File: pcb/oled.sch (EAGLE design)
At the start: 20 parts, among them U1 UG-2828GDEDF11, U2 FAN5331SX

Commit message: changed part number for pin header on oled board
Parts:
- JP1, JP2: BOTTOM (none) -> 0; MPN 10129378-908001BLF -> C124381; POPULATE 0 -> 1; THRU-HOLE (none) -> 1
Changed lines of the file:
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@@
 <?xml version="1.0" encoding="utf-8"?>
 <!DOCTYPE eagle SYSTEM "eagle.dtd">
-<eagle version="9.6.2">
+<eagle version="9.5.0">
 <drawing>
 <settings>
@@
 </part>
 <part name="JP2" library="adafruit" library_urn="urn:adsk.eagle:library:420" deviceset="PINHD-1X8" device="CLEANBIG" package3d_urn="urn:adsk.eagle:package:6240708/1" override_package3d_urn="urn:adsk.eagle:package:21520305/2" override_package_urn="urn:adsk.eagle:footprint:6240062/1">
-<attribute name="MPN" value="10129378-908001BLF"/>
-<attribute name="POPULATE" value="0"/>
+<attribute name="BOTTOM" value="0"/>
+<attribute name="MPN" value="C124381"/>
+<attribute name="POPULATE" value="1"/>
+<attribute name="THRU-HOLE" value="1"/>
 </part>
 <part name="JP1" library="adafruit" library_urn="urn:adsk.eagle:library:420" deviceset="PINHD-1X8" device="CLEANBIG" package3d_urn="urn:adsk.eagle:package:6240708/1" override_package3d_urn="urn:adsk.eagle:package:21520308/2" override_package_urn="urn:adsk.eagle:footprint:6240062/1">
-<attribute name="MPN" value="10129378-908001BLF"/>
-<attribute name="POPULATE" value="0"/>
+<attribute name="BOTTOM" value="0"/>
+<attribute name="MPN" value="C124381"/>
+<attribute name="POPULATE" value="1"/>
+<attribute name="THRU-HOLE" value="1"/>
 </part>
 <part name="SUPPLY1" library="SparkFun-PowerSymbols" library_urn="urn:adsk.eagle:library:530" deviceset="VIN" device=""/>
@@
 <attribute name="POPULATE" x="226.06" y="91.44" size="1.778" layer="96" rot="R180" display="off"/>
 <attribute name="MPN" x="226.06" y="91.44" size="1.778" layer="96" rot="R180" display="off"/>
+<attribute name="THRU-HOLE" x="226.06" y="91.44" size="1.778" layer="96" rot="R180" display="off"/>
+<attribute name="BOTTOM" x="226.06" y="91.44" size="1.778" layer="96" rot="R180" display="off"/>
 </instance>
 <instance part="JP1" gate="G$1" x="215.9" y="93.98" smashed="yes">
@@
 <attribute name="POPULATE" x="215.9" y="93.98" size="1.778" layer="96" display="off"/>
 <attribute name="MPN" x="215.9" y="93.98" size="1.778" layer="96" display="off"/>
+<attribute name="THRU-HOLE" x="215.9" y="93.98" size="1.778" layer="96" display="off"/>
+<attribute name="BOTTOM" x="215.9" y="93.98" size="1.778" layer="96" display="off"/>
 </instance>
 <instance part="SUPPLY1" gate="G$1" x="193.04" y="177.8" smashed="yes">

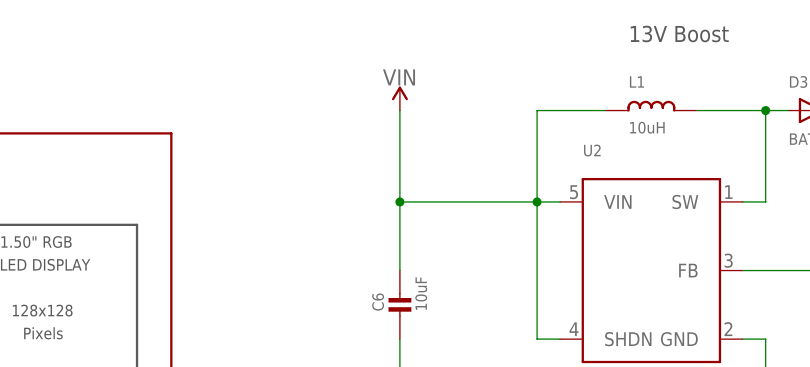
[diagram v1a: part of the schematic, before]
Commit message: Revert OLED board to use 3.3V for input to the 13V FAN5331 boost
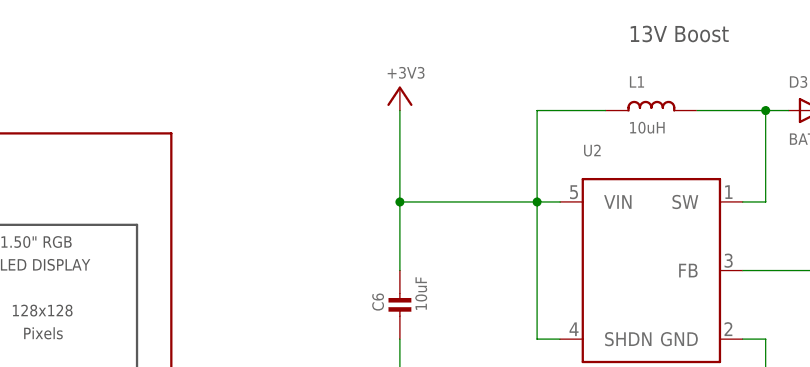
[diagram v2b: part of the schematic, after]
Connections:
- net +3V3: now also C6.P$1, L1.1, U2.SHDN, U2.VIN
- net VIN: no longer C6.P$1, L1.1, U2.SHDN, U2.VIN
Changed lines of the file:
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@@
 <?xml version="1.0" encoding="utf-8"?>
 <!DOCTYPE eagle SYSTEM "eagle.dtd">
-<eagle version="9.5.0">
+<eagle version="9.6.2">
 <drawing>
 <settings>
@@
 <attribute name="THRU-HOLE" value="1"/>
 </part>
-<part name="SUPPLY1" library="SparkFun-PowerSymbols" library_urn="urn:adsk.eagle:library:530" deviceset="VIN" device=""/>
+<part name="+3V1" library="supply1" library_urn="urn:adsk.eagle:library:371" deviceset="+3V3" device=""/>
 </parts>
 <sheets>
@@
 <attribute name="BOTTOM" x="215.9" y="93.98" size="1.778" layer="96" display="off"/>
 </instance>
-<instance part="SUPPLY1" gate="G$1" x="193.04" y="177.8" smashed="yes">
-<attribute name="VALUE" x="193.04" y="180.594" size="1.778" layer="96" align="bottom-center"/>
+<instance part="+3V1" gate="G$1" x="193.04" y="180.34" smashed="yes">
+<attribute name="VALUE" x="191.516" y="181.356" size="1.27" layer="96"/>
 </instance>
 </instances>
@@
 <pinref part="U1" gate="G$1" pin="VCI"/>
 </segment>
-</net>
-<net name="D1/GPIO5" class="0">
-<segment>
-<pinref part="JP1" gate="G$1" pin="3"/>
-<wire x1="213.36" y1="96.52" x2="203.2" y2="96.52" width="0.1524" layer="91"/>
-<label x="203.2" y="96.52" size="1.778" layer="95" rot="R180"/>
-</segment>
-</net>
-<net name="D2/GPIO4" class="0">
-<segment>
-<pinref part="JP1" gate="G$1" pin="4"/>
-<wire x1="213.36" y1="93.98" x2="203.2" y2="93.98" width="0.1524" layer="91"/>
-<label x="203.2" y="93.98" size="1.778" layer="95" rot="R180"/>
-</segment>
-</net>
-<net name="D3/GPIO0" class="0">
-<segment>
-<pinref part="JP1" gate="G$1" pin="5"/>
-<wire x1="213.36" y1="91.44" x2="203.2" y2="91.44" width="0.1524" layer="91"/>
-<label x="203.2" y="91.44" size="1.778" layer="95" rot="R180"/>
-</segment>
-</net>
-<net name="D4/GPIO2" class="0">
-<segment>
-<pinref part="JP1" gate="G$1" pin="6"/>
-<wire x1="213.36" y1="88.9" x2="203.2" y2="88.9" width="0.1524" layer="91"/>
-<label x="203.2" y="88.9" size="1.778" layer="95" rot="R180"/>
-</segment>
-<segment>
-<wire x1="129.54" y1="124.46" x2="111.76" y2="124.46" width="0.1524" layer="91"/>
-<label x="111.76" y="124.46" size="1.778" layer="95"/>
-<pinref part="U1" gate="G$1" pin="D/C#"/>
-</segment>
-</net>
-<net name="D8/GPIO15" class="0">
-<segment>
-<pinref part="JP2" gate="G$1" pin="2"/>
-<wire x1="228.6" y1="86.36" x2="238.76" y2="86.36" width="0.1524" layer="91"/>
-<label x="238.76" y="86.36" size="1.778" layer="95"/>
-</segment>
-<segment>
-<wire x1="129.54" y1="121.92" x2="111.76" y2="121.92" width="0.1524" layer="91"/>
-<label x="111.76" y="121.92" size="1.778" layer="95"/>
-<pinref part="U1" gate="G$1" pin="RES#"/>
-</segment>
-</net>
-<net name="D5/GPIO14/SCK" class="0">
-<segment>
-<pinref part="JP2" gate="G$1" pin="5"/>
-<wire x1="228.6" y1="93.98" x2="238.76" y2="93.98" width="0.1524" layer="91"/>
-<label x="238.76" y="93.98" size="1.778" layer="95"/>
-</segment>
-<segment>
-<wire x1="129.54" y1="139.7" x2="111.76" y2="139.7" width="0.1524" layer="91"/>
-<label x="111.76" y="139.7" size="1.778" layer="95"/>
-<pinref part="U1" gate="G$1" pin="D0/SCK"/>
-</segment>
-</net>
-<net name="D0/GPIO16" class="0">
-<segment>
-<pinref part="JP2" gate="G$1" pin="6"/>
-<wire x1="228.6" y1="96.52" x2="238.76" y2="96.52" width="0.1524" layer="91"/>
-<label x="238.76" y="96.52" size="1.778" layer="95"/>
-</segment>
-<segment>
-<wire x1="129.54" y1="127" x2="111.76" y2="127" width="0.1524" layer="91"/>
-<label x="111.76" y="127" size="1.778" layer="95"/>
-<pinref part="U1" gate="G$1" pin="CS#"/>
-</segment>
-</net>
-<net name="A0" class="0">
-<segment>
-<pinref part="JP2" gate="G$1" pin="7"/>
-<wire x1="228.6" y1="99.06" x2="238.76" y2="99.06" width="0.1524" layer="91"/>
-<label x="238.76" y="99.06" size="1.778" layer="95"/>
-</segment>
-</net>
-<net name="D7/GPIO13/MOSI" class="0">
-<segment>
-<pinref part="JP2" gate="G$1" pin="3"/>
-<wire x1="228.6" y1="88.9" x2="238.76" y2="88.9" width="0.1524" layer="91"/>
-<label x="238.76" y="88.9" size="1.778" layer="95"/>
-</segment>
-<segment>
-<wire x1="129.54" y1="142.24" x2="111.76" y2="142.24" width="0.1524" layer="91"/>
-<label x="111.76" y="142.24" size="1.778" layer="95"/>
-<pinref part="U1" gate="G$1" pin="D1/SDIN"/>
-</segment>
-</net>
-<net name="VIN" class="1">
 <segment>
 <wire x1="193.04" y1="167.64" x2="193.04" y2="160.02" width="0.1524" layer="91"/>
@@
 <pinref part="U2" gate="G$1" pin="SHDN"/>
 <pinref part="L1" gate="G$1" pin="1"/>
-<pinref part="SUPPLY1" gate="G$1" pin="VIN"/>
-</segment>
+<pinref part="+3V1" gate="G$1" pin="+3V3"/>
+</segment>
+</net>
+<net name="D1/GPIO5" class="0">
+<segment>
+<pinref part="JP1" gate="G$1" pin="3"/>
+<wire x1="213.36" y1="96.52" x2="203.2" y2="96.52" width="0.1524" layer="91"/>
+<label x="203.2" y="96.52" size="1.778" layer="95" rot="R180"/>
+</segment>
+</net>
+<net name="D2/GPIO4" class="0">
+<segment>
+<pinref part="JP1" gate="G$1" pin="4"/>
+<wire x1="213.36" y1="93.98" x2="203.2" y2="93.98" width="0.1524" layer="91"/>
+<label x="203.2" y="93.98" size="1.778" layer="95" rot="R180"/>
+</segment>
+</net>
+<net name="D3/GPIO0" class="0">
+<segment>
+<pinref part="JP1" gate="G$1" pin="5"/>
+<wire x1="213.36" y1="91.44" x2="203.2" y2="91.44" width="0.1524" layer="91"/>
+<label x="203.2" y="91.44" size="1.778" layer="95" rot="R180"/>
+</segment>
+</net>
+<net name="D4/GPIO2" class="0">
+<segment>
+<pinref part="JP1" gate="G$1" pin="6"/>
+<wire x1="213.36" y1="88.9" x2="203.2" y2="88.9" width="0.1524" layer="91"/>
+<label x="203.2" y="88.9" size="1.778" layer="95" rot="R180"/>
+</segment>
+<segment>
+<wire x1="129.54" y1="124.46" x2="111.76" y2="124.46" width="0.1524" layer="91"/>
+<label x="111.76" y="124.46" size="1.778" layer="95"/>
+<pinref part="U1" gate="G$1" pin="D/C#"/>
+</segment>
+</net>
+<net name="D8/GPIO15" class="0">
+<segment>
+<pinref part="JP2" gate="G$1" pin="2"/>
+<wire x1="228.6" y1="86.36" x2="238.76" y2="86.36" width="0.1524" layer="91"/>
+<label x="238.76" y="86.36" size="1.778" layer="95"/>
+</segment>
+<segment>
+<wire x1="129.54" y1="121.92" x2="111.76" y2="121.92" width="0.1524" layer="91"/>
+<label x="111.76" y="121.92" size="1.778" layer="95"/>
+<pinref part="U1" gate="G$1" pin="RES#"/>
+</segment>
+</net>
+<net name="D5/GPIO14/SCK" class="0">
+<segment>
+<pinref part="JP2" gate="G$1" pin="5"/>
+<wire x1="228.6" y1="93.98" x2="238.76" y2="93.98" width="0.1524" layer="91"/>
+<label x="238.76" y="93.98" size="1.778" layer="95"/>
+</segment>
+<segment>
+<wire x1="129.54" y1="139.7" x2="111.76" y2="139.7" width="0.1524" layer="91"/>
+<label x="111.76" y="139.7" size="1.778" layer="95"/>
+<pinref part="U1" gate="G$1" pin="D0/SCK"/>
+</segment>
+</net>
+<net name="D0/GPIO16" class="0">
+<segment>
+<pinref part="JP2" gate="G$1" pin="6"/>
+<wire x1="228.6" y1="96.52" x2="238.76" y2="96.52" width="0.1524" layer="91"/>
+<label x="238.76" y="96.52" size="1.778" layer="95"/>
+</segment>
+<segment>
+<wire x1="129.54" y1="127" x2="111.76" y2="127" width="0.1524" layer="91"/>
+<label x="111.76" y="127" size="1.778" layer="95"/>
+<pinref part="U1" gate="G$1" pin="CS#"/>
+</segment>
+</net>
+<net name="A0" class="0">
+<segment>
+<pinref part="JP2" gate="G$1" pin="7"/>
+<wire x1="228.6" y1="99.06" x2="238.76" y2="99.06" width="0.1524" layer="91"/>
+<label x="238.76" y="99.06" size="1.778" layer="95"/>
+</segment>
+</net>
+<net name="D7/GPIO13/MOSI" class="0">
+<segment>
+<pinref part="JP2" gate="G$1" pin="3"/>
+<wire x1="228.6" y1="88.9" x2="238.76" y2="88.9" width="0.1524" layer="91"/>
+<label x="238.76" y="88.9" size="1.778" layer="95"/>
+</segment>
+<segment>
+<wire x1="129.54" y1="142.24" x2="111.76" y2="142.24" width="0.1524" layer="91"/>
+<label x="111.76" y="142.24" size="1.778" layer="95"/>
+<pinref part="U1" gate="G$1" pin="D1/SDIN"/>
+</segment>
+</net>
+<net name="VIN" class="1">
 <segment>
 <pinref part="JP1" gate="G$1" pin="8"/>

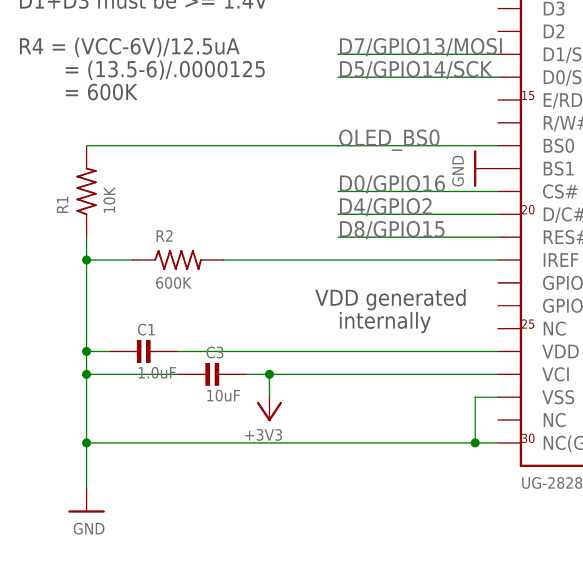
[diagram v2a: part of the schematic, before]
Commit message: changed 590k resistor to 620k
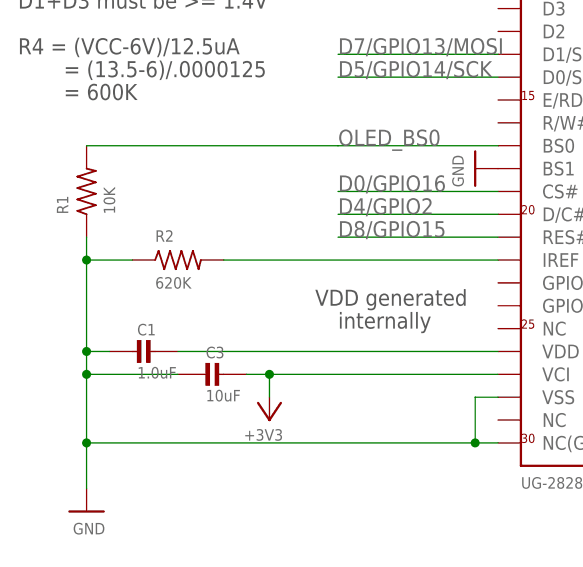
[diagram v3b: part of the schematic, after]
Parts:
- R2: value 600K -> 620K; MPN ERJ-6ENF5903V -> 0805W8F6203T5E
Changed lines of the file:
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@@
 <?xml version="1.0" encoding="utf-8"?>
 <!DOCTYPE eagle SYSTEM "eagle.dtd">
-<eagle version="9.6.2">
+<eagle version="9.5.0">
 <drawing>
 <settings>
@@
 <parts>
 <part name="GND2" library="supply1" library_urn="urn:adsk.eagle:library:371" deviceset="GND" device=""/>
-<part name="R2" library="adafruit" library_urn="urn:adsk.eagle:library:420" deviceset="R-US_" device="R0805" package3d_urn="urn:adsk.eagle:package:6240566/1" override_package3d_urn="urn:adsk.eagle:package:21520237/2" override_package_urn="urn:adsk.eagle:footprint:6239920/1" value="600K">
-<attribute name="MPN" value="ERJ-6ENF5903V"/>
+<part name="R2" library="adafruit" library_urn="urn:adsk.eagle:library:420" deviceset="R-US_" device="R0805" package3d_urn="urn:adsk.eagle:package:6240566/1" override_package3d_urn="urn:adsk.eagle:package:21520237/2" override_package_urn="urn:adsk.eagle:footprint:6239920/1" value="620K">
+<attribute name="MPN" value="0805W8F6203T5E"/>
 </part>
 <part name="C2" library="microbuilder" deviceset="CAP_CERAMIC" device="0805" override_package3d_urn="urn:adsk.eagle:package:21520266/2" override_package_urn="urn:adsk.eagle:footprint:21520267/1" value="10uF/16V">
